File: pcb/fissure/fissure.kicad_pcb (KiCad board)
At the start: 2 copper layers, 127.6 x 94 mm, 145 parts, among them J1 AudioJack4, J2 AudioJack4, J3 Conn_01x04, J4 Conn_01x04, J5 Conn_01x03, J6 Conn_01x03, J7 Conn_01x04, J8 Conn_01x04, J9 Conn_01x04, K1 KEYSW, K10 KEYSW, K11 KEYSW, K12 KEYSW, K13 KEYSW, K14 KEYSW, K15 KEYSW, K16 KEYSW, K17 KEYSW, K18 KEYSW, K19 KEYSW, K2 KEYSW, K20 KEYSW, K3 KEYSW, K4 KEYSW, K5 KEYSW, K6 KEYSW, K7 KEYSW, K8 KEYSW, K9 KEYSW, SW1 SW_PUSH, U1 ProMicro, U2 MT25QL128ABA1ESE, U3 MT25QL128ABA1ESE

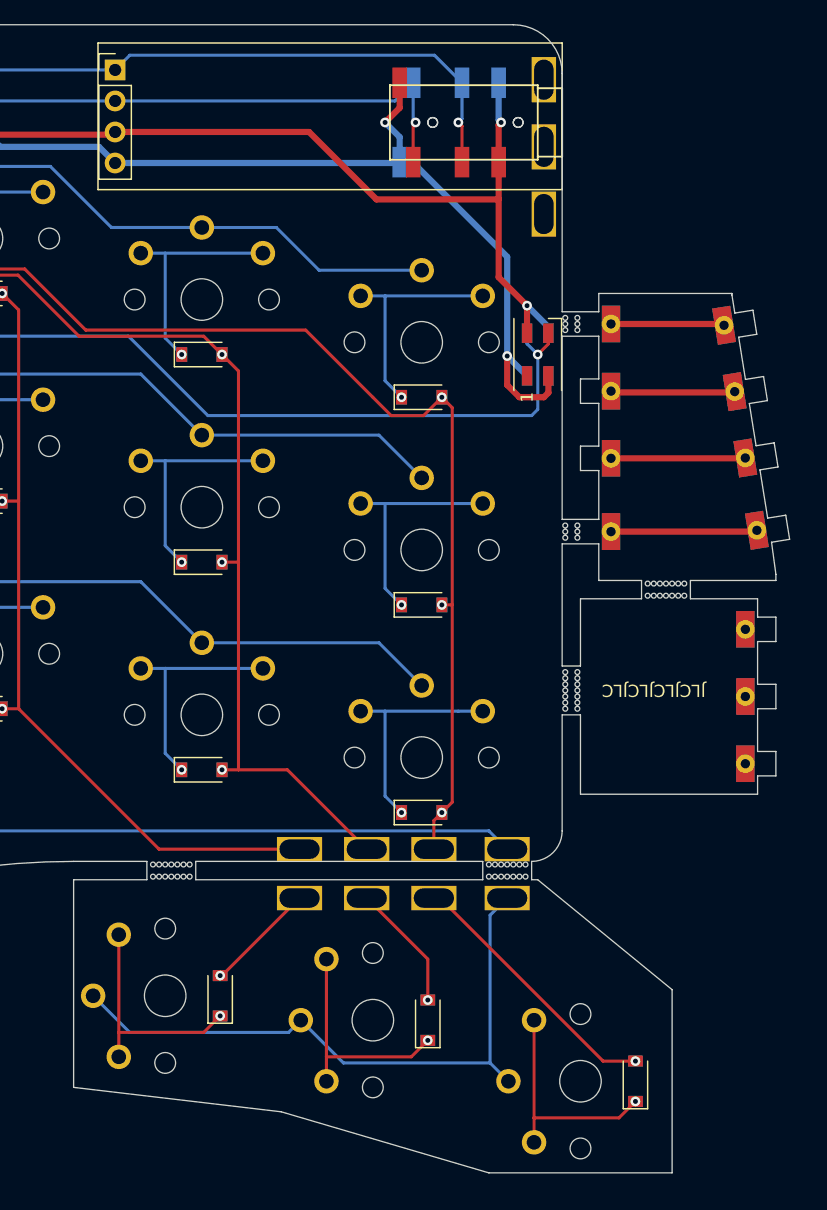
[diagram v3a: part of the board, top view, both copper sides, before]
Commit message: Change to using large breakaway holes
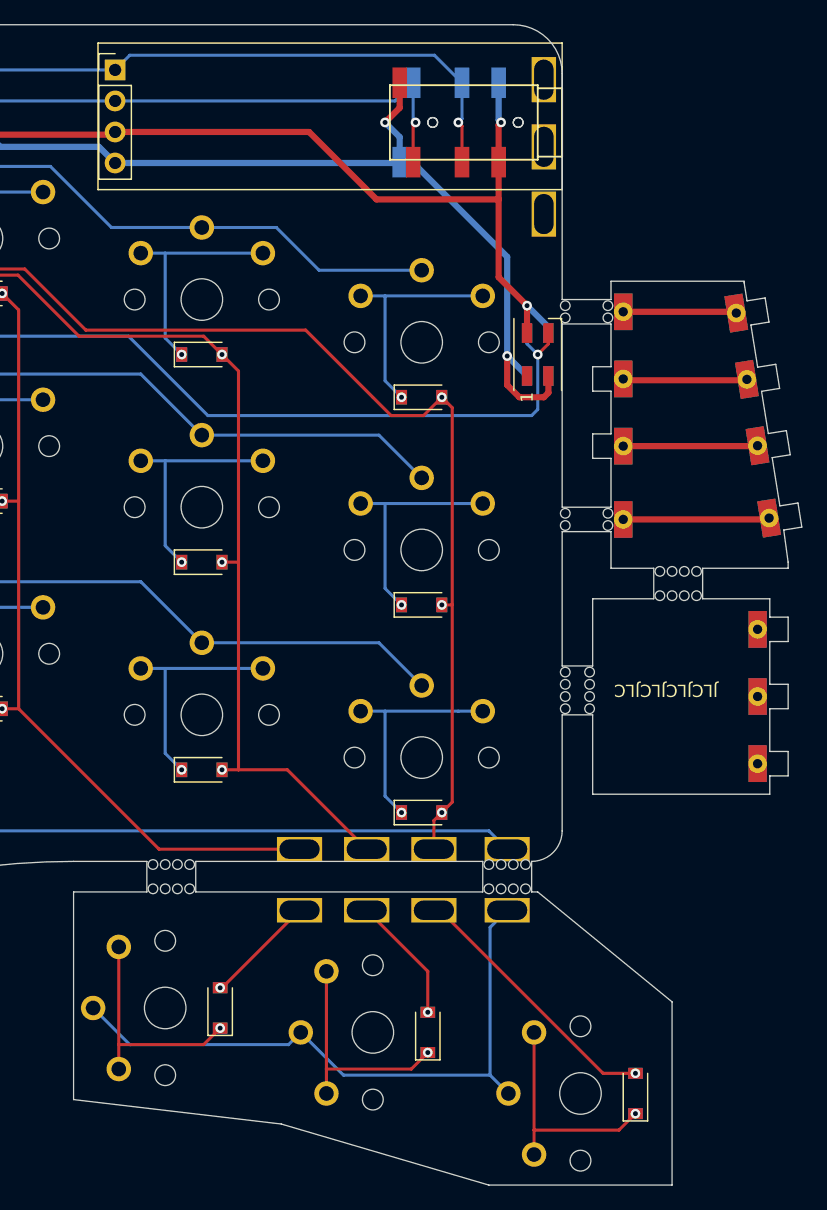
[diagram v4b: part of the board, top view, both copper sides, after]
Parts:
- removed the REF** at (143.0, 90.5)
- removed the REF** at (142.0, 92.0)
- removed the REF** at (142.5, 92.0)
- removed the REF** at (145.0, 92.0)
- removed the REF** at (143.5, 92.0)
- removed the REF** at (144.5, 92.0)
- removed the REF** at (136.5, 99.0)
- removed the REF** at (136.5, 100.0)
- removed the REF** at (136.5, 101.0)
- removed the REF** at (136.5, 100.5)
- removed the REF** at (136.5, 98.0)
- removed the REF** at (144.0, 90.5)
- removed the REF** at (136.5, 99.5)
- removed the REF** at (136.5, 98.5)
- removed the REF** at (135.0, 100.0)
- removed the REF** at (135.0, 99.0)
- removed the REF** at (135.0, 98.0)
- removed the REF** at (135.0, 98.5)
- removed the REF** at (135.0, 101.0)
- removed the REF** at (135.0, 99.5)
- removed the REF** at (135.0, 100.5)
- removed the REF** at (131.0, 115.0)
- removed the REF** at (145.0, 90.5)
- removed the REF** at (130.0, 115.0)
- removed the REF** at (129.0, 115.0)
- removed the REF** at (129.5, 115.0)
- removed the REF** at (132.0, 115.0)
- removed the REF** at (130.5, 115.0)
- removed the REF** at (131.5, 115.0)
- removed the REF** at (130.0, 113.5)
- removed the REF** at (131.0, 113.5)
- removed the REF** at (132.0, 113.5)
- removed the REF** at (131.5, 113.5)
- removed the REF** at (144.5, 90.5)
- removed the REF** at (129.0, 113.5)
- removed the REF** at (130.5, 113.5)
- removed the REF** at (129.5, 113.5)
- removed the REF** at (103.5, 115.0)
- removed the REF** at (102.5, 115.0)
- removed the REF** at (101.5, 115.0)
- removed the REF** at (102.0, 115.0)
- removed the REF** at (104.5, 115.0)
- removed the REF** at (103.0, 115.0)
- removed the REF** at (104.0, 115.0)
- removed the REF** at (142.0, 90.5)
- removed the REF** at (104.0, 113.5)
- removed the REF** at (103.0, 113.5)
- removed the REF** at (102.0, 113.5)
- removed the REF** at (104.5, 113.5)
- removed the REF** at (101.5, 113.5)
- removed the REF** at (135.0, 69.5)
- removed the REF** at (136.5, 69.5)
- removed the REF** at (135.0, 86.5)
- removed the REF** at (136.5, 86.5)
- removed the REF** at (103.5, 113.5)
- removed the REF** at (143.5, 90.5)
- removed the REF** at (102.5, 113.5)
- removed the REF** at (136.5, 70.0)
- removed the REF** at (135.0, 69.0)
- removed the REF** at (136.5, 69.0)
- removed the REF** at (135.0, 70.0)
- removed the REF** at (135.0, 86.0)
- removed the REF** at (135.0, 87.0)
- removed the REF** at (136.5, 86.0)
- removed the REF** at (136.5, 87.0)
- removed the REF** at (142.5, 90.5)
- removed the REF** at (144.0, 92.0)
- removed the REF** at (143.0, 92.0)
- added REF**: breakaway-hole-big, Keebio-Parts:breakaway-hole-big, F.Cu at (139.0, 69.0)
- added REF**: breakaway-hole-big, Keebio-Parts:breakaway-hole-big, F.Cu at (145.0, 89.5)
- added REF**: breakaway-hole-big, Keebio-Parts:breakaway-hole-big, F.Cu at (144.0, 89.5)
- added REF**: breakaway-hole-big, Keebio-Parts:breakaway-hole-big, F.Cu at (146.0, 89.5)
- added REF**: breakaway-hole-big, Keebio-Parts:breakaway-hole-big, F.Cu at (146.0, 92.0)
- added REF**: breakaway-hole-big, Keebio-Parts:breakaway-hole-big, F.Cu at (144.0, 92.0)
- added REF**: breakaway-hole-big, Keebio-Parts:breakaway-hole-big, F.Cu at (145.0, 92.0)
- added REF**: breakaway-hole-big, Keebio-Parts:breakaway-hole-big, F.Cu at (143.0, 92.0)
- added REF**: breakaway-hole-big, Keebio-Parts:breakaway-hole-big, F.Cu at (135.0, 101.0)
- added REF**: breakaway-hole-big, Keebio-Parts:breakaway-hole-big, F.Cu at (135.0, 99.0)
- added REF**: breakaway-hole-big, Keebio-Parts:breakaway-hole-big, F.Cu at (135.0, 100.0)
- added REF**: breakaway-hole-big, Keebio-Parts:breakaway-hole-big, F.Cu at (139.0, 68.0)
- added REF**: breakaway-hole-big, Keebio-Parts:breakaway-hole-big, F.Cu at (135.0, 98.0)
- added REF**: breakaway-hole-big, Keebio-Parts:breakaway-hole-big, F.Cu at (137.5, 98.0)
- added REF**: breakaway-hole-big, Keebio-Parts:breakaway-hole-big, F.Cu at (137.5, 100.0)
- added REF**: breakaway-hole-big, Keebio-Parts:breakaway-hole-big, F.Cu at (137.5, 99.0)
- added REF**: breakaway-hole-big, Keebio-Parts:breakaway-hole-big, F.Cu at (137.5, 101.0)
- added REF**: breakaway-hole-big, Keebio-Parts:breakaway-hole-big, F.Cu at (129.0, 113.5)
- added REF**: breakaway-hole-big, Keebio-Parts:breakaway-hole-big, F.Cu at (131.0, 113.5)
- added REF**: breakaway-hole-big, Keebio-Parts:breakaway-hole-big, F.Cu at (130.0, 113.5)
- added REF**: breakaway-hole-big, Keebio-Parts:breakaway-hole-big, F.Cu at (132.0, 113.5)
- added REF**: breakaway-hole-big, Keebio-Parts:breakaway-hole-big, F.Cu at (132.0, 116.0)
- added REF**: breakaway-hole-big, Keebio-Parts:breakaway-hole-big, F.Cu at (135.0, 68.0)
- added REF**: breakaway-hole-big, Keebio-Parts:breakaway-hole-big, F.Cu at (130.0, 116.0)
- added REF**: breakaway-hole-big, Keebio-Parts:breakaway-hole-big, F.Cu at (131.0, 116.0)
- added REF**: breakaway-hole-big, Keebio-Parts:breakaway-hole-big, F.Cu at (129.0, 116.0)
- added REF**: breakaway-hole-big, Keebio-Parts:breakaway-hole-big, F.Cu at (104.5, 116.0)
- added REF**: breakaway-hole-big, Keebio-Parts:breakaway-hole-big, F.Cu at (103.5, 116.0)
- added REF**: breakaway-hole-big, Keebio-Parts:breakaway-hole-big, F.Cu at (102.5, 116.0)
- added REF**: breakaway-hole-big, Keebio-Parts:breakaway-hole-big, F.Cu at (101.5, 116.0)
- added REF**: breakaway-hole-big, Keebio-Parts:breakaway-hole-big, F.Cu at (104.5, 113.5)
- added REF**: breakaway-hole-big, Keebio-Parts:breakaway-hole-big, F.Cu at (103.5, 113.5)
- added REF**: breakaway-hole-big, Keebio-Parts:breakaway-hole-big, F.Cu at (102.5, 113.5)
- added REF**: breakaway-hole-big, Keebio-Parts:breakaway-hole-big, F.Cu at (135.0, 69.0)
- added REF**: breakaway-hole-big, Keebio-Parts:breakaway-hole-big, F.Cu at (101.5, 113.5)
- added REF**: breakaway-hole-big, Keebio-Parts:breakaway-hole-big, F.Cu at (139.0, 86.0)
- added REF**: breakaway-hole-big, Keebio-Parts:breakaway-hole-big, F.Cu at (139.0, 85.0)
- added REF**: breakaway-hole-big, Keebio-Parts:breakaway-hole-big, F.Cu at (135.0, 86.0)
- added REF**: breakaway-hole-big, Keebio-Parts:breakaway-hole-big, F.Cu at (135.0, 85.0)
- added REF**: breakaway-hole-big, Keebio-Parts:breakaway-hole-big, F.Cu at (143.0, 89.5)
- moved J7 1.41 mm to (140.0, 77.0)
- moved J8 1.41 mm to (150.6, 77.0)
- moved D35 1.00 mm to (107.0, 125.5)
- moved D36 1.00 mm to (107.0, 125.5)
- moved D37 1.00 mm to (124.0, 127.5)
- moved D38 1.00 mm to (124.0, 127.5)
- moved D39 1.00 mm to (141.0, 132.5)
- moved D40 1.00 mm to (141.0, 132.5)
- moved J4 1.00 mm to (121.5, 117.5)
- moved J5 1.00 mm to (151.0, 100.0)
- moved K18 1.00 mm to (102.5, 125.5)
- moved K19 1.00 mm to (119.5, 127.5)
- moved K20 1.00 mm to (136.5, 132.5)
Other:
- board size 127.6 x 94 mm -> 128.6 x 95 mm

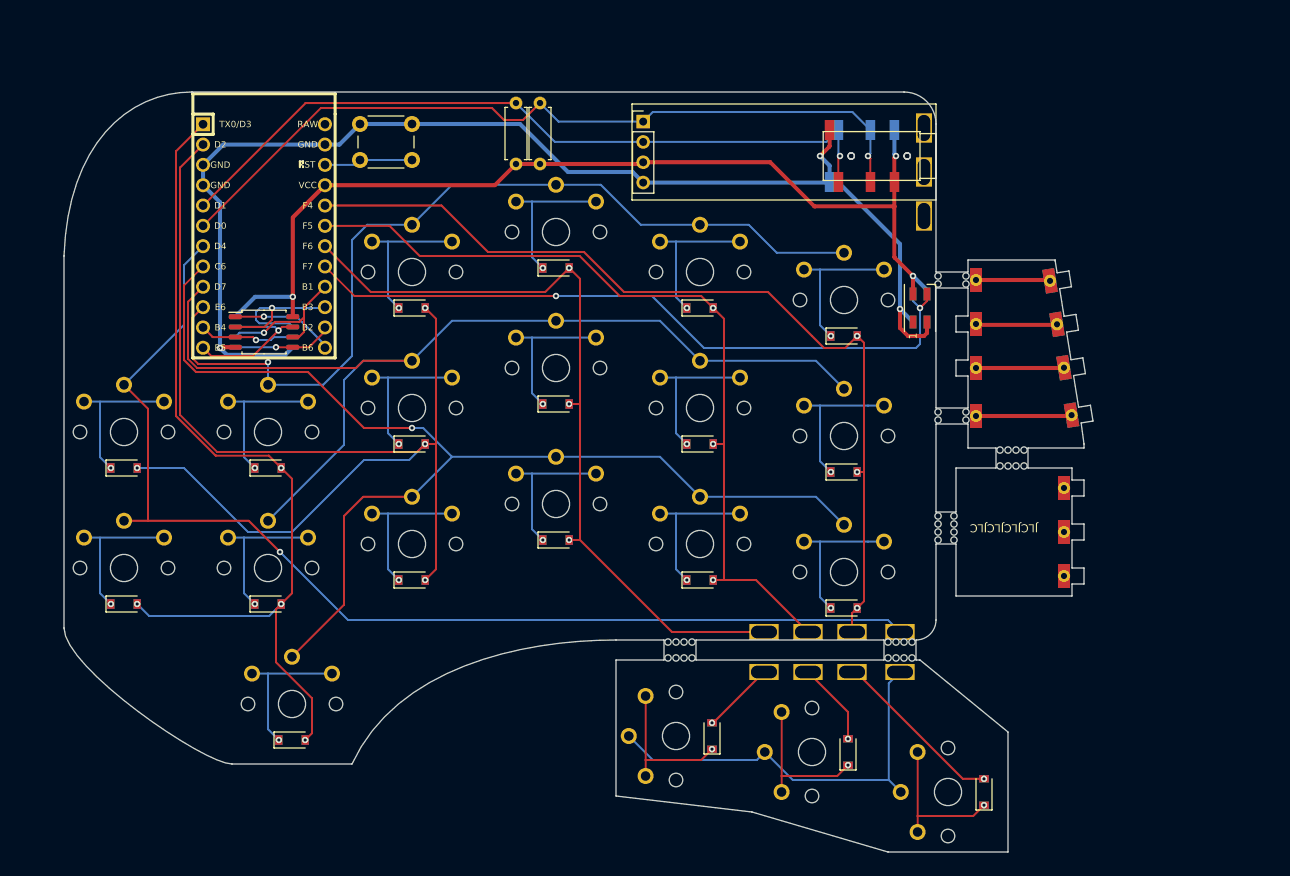
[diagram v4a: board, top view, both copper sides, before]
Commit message: Use nice!nano
- Add nice!nano symbols and footprints
- Move DQ2,3 to extra pins (to leave room for future analog stick?)
- Improved a bit of general routing
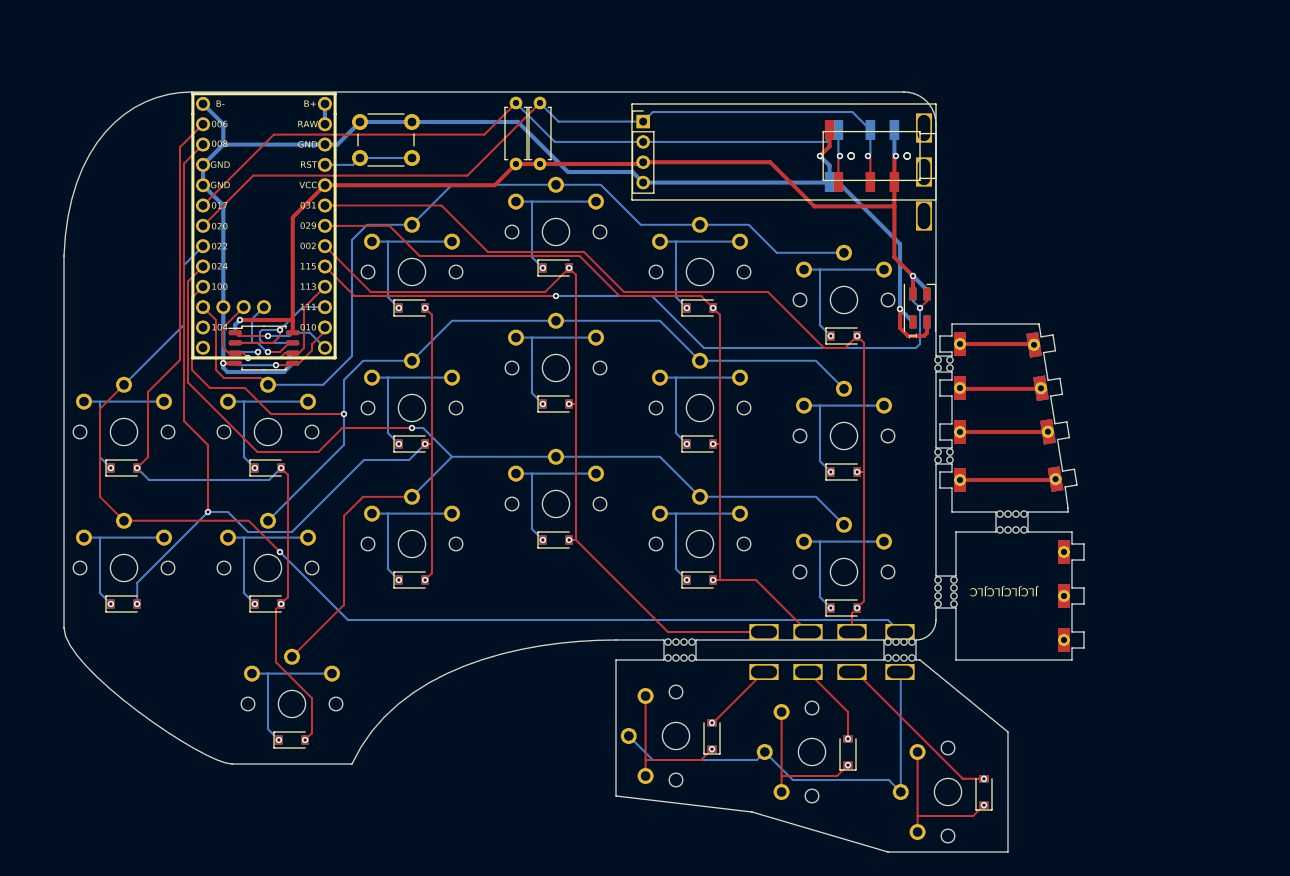
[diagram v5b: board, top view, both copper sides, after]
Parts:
- removed the REF** at (139.0, 69.0)
- removed the REF** at (145.0, 89.5)
- removed the REF** at (144.0, 89.5)
- removed the REF** at (146.0, 89.5)
- removed the REF** at (146.0, 92.0)
- removed the REF** at (144.0, 92.0)
- removed the REF** at (145.0, 92.0)
- removed the REF** at (143.0, 92.0)
- removed the REF** at (135.0, 101.0)
- removed the REF** at (135.0, 99.0)
- removed the REF** at (135.0, 100.0)
- removed the REF** at (139.0, 68.0)
- removed the REF** at (135.0, 98.0)
- removed the REF** at (137.5, 98.0)
- removed the REF** at (137.5, 100.0)
- removed the REF** at (137.5, 99.0)
- removed the REF** at (137.5, 101.0)
- removed the REF** at (135.0, 68.0)
- removed the REF** at (135.0, 69.0)
- removed the REF** at (139.0, 86.0)
- removed the REF** at (139.0, 85.0)
- removed the REF** at (135.0, 86.0)
- removed the REF** at (135.0, 85.0)
- removed the REF** at (143.0, 89.5)
- added REF**: breakaway-hole-big, Keebio-Parts:breakaway-hole-big, F.Cu at (137.0, 90.0)
- added REF**: breakaway-hole-big, Keebio-Parts:breakaway-hole-big, F.Cu at (145.0, 97.5)
- added REF**: breakaway-hole-big, Keebio-Parts:breakaway-hole-big, F.Cu at (144.0, 97.5)
- added REF**: breakaway-hole-big, Keebio-Parts:breakaway-hole-big, F.Cu at (146.0, 97.5)
- added REF**: breakaway-hole-big, Keebio-Parts:breakaway-hole-big, F.Cu at (146.0, 100.0)
- added REF**: breakaway-hole-big, Keebio-Parts:breakaway-hole-big, F.Cu at (144.0, 100.0)
- added REF**: breakaway-hole-big, Keebio-Parts:breakaway-hole-big, F.Cu at (145.0, 100.0)
- added REF**: breakaway-hole-big, Keebio-Parts:breakaway-hole-big, F.Cu at (143.0, 100.0)
- added REF**: breakaway-hole-big, Keebio-Parts:breakaway-hole-big, F.Cu at (135.0, 109.0)
- added REF**: breakaway-hole-big, Keebio-Parts:breakaway-hole-big, F.Cu at (135.0, 107.0)
- added REF**: breakaway-hole-big, Keebio-Parts:breakaway-hole-big, F.Cu at (135.0, 108.0)
- added REF**: breakaway-hole-big, Keebio-Parts:breakaway-hole-big, F.Cu at (137.0, 91.0)
- added REF**: breakaway-hole-big, Keebio-Parts:breakaway-hole-big, F.Cu at (135.0, 106.0)
- added REF**: breakaway-hole-big, Keebio-Parts:breakaway-hole-big, F.Cu at (137.5, 106.0)
- added REF**: breakaway-hole-big, Keebio-Parts:breakaway-hole-big, F.Cu at (137.5, 108.0)
- added REF**: breakaway-hole-big, Keebio-Parts:breakaway-hole-big, F.Cu at (137.5, 107.0)
- added REF**: breakaway-hole-big, Keebio-Parts:breakaway-hole-big, F.Cu at (137.5, 109.0)
- added REF**: breakaway-hole-big, Keebio-Parts:breakaway-hole-big, F.Cu at (135.0, 91.0)
- added REF**: breakaway-hole-big, Keebio-Parts:breakaway-hole-big, F.Cu at (135.0, 90.0)
- added REF**: breakaway-hole-big, Keebio-Parts:breakaway-hole-big, F.Cu at (135.0, 78.5)
- added REF**: breakaway-hole-big, Keebio-Parts:breakaway-hole-big, F.Cu at (135.0, 79.5)
- added REF**: breakaway-hole-big, Keebio-Parts:breakaway-hole-big, F.Cu at (137.0, 78.5)
- added REF**: breakaway-hole-big, Keebio-Parts:breakaway-hole-big, F.Cu at (137.0, 79.5)
- added REF**: breakaway-hole-big, Keebio-Parts:breakaway-hole-big, F.Cu at (143.0, 97.5)
- U1: value ProMicro -> nice_nano; footprint Keebio-Parts:ArduinoProMicro -> nice-nano-kicad:nice_nano
- moved D31 17.0 mm to (33.5, 92.0)
- moved D32 17.0 mm to (33.5, 92.0)
- moved D33 17.0 mm to (33.5, 109.0)
- moved D34 17.0 mm to (33.5, 109.0)
- moved K16 17.0 mm to (33.5, 87.5)
- moved K17 17.0 mm to (33.5, 104.5)
- moved J7 8.25 mm to (138.0, 85.0)
- moved J8 8.25 mm to (148.6, 85.0)
- moved J5 8.00 mm to (151.0, 108.0)
- moved U2 2.00 mm to (51.0, 77.0)
- moved U3 2.00 mm to (51.0, 77.0)
- moved SW1 0.25 mm to (63.0, 48.8)
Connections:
- U1 pad 11: DQ2 -> Net-(U1-Pad11)
- U1 pad 12: DQ3 -> Net-(U1-Pad12)
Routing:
- net COL2: track 148.3 -> 131.6 mm, vias 4 -> 5
- net GND: track 156.7 -> 164.7 mm
- net COL1: track 110.6 -> 102.8 mm
- net ROW2: track 129.3 -> 122.9 mm, vias 0 -> 1
- net DQ3: track 18.7 -> 13.3 mm
- net ROW1: track 114.0 -> 110.2 mm, vias 1 -> 0
- net DQ2: track 12.0 -> 15.6 mm
- net ROW3: track 140.6 -> 144.0 mm
- net RAW: track 0.00 -> 2.54 mm
- net VCC: track 125.6 -> 127.7 mm
- net MOSI_DQ0: track 12.5 -> 14.0 mm
- net ROW4: track 142.4 -> 143.7 mm
- net SDA: track 100.2 -> 98.9 mm
- net Net-(J4-Pad4): track 51.8 -> 52.8 mm
- net COL4: track 103.2 -> 102.5 mm
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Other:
- board size 128.6 x 95 mm -> 127.5 x 95 mm
